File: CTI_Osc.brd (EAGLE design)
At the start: 53 x 45 mm, 15 parts, among them IC6 7805DT

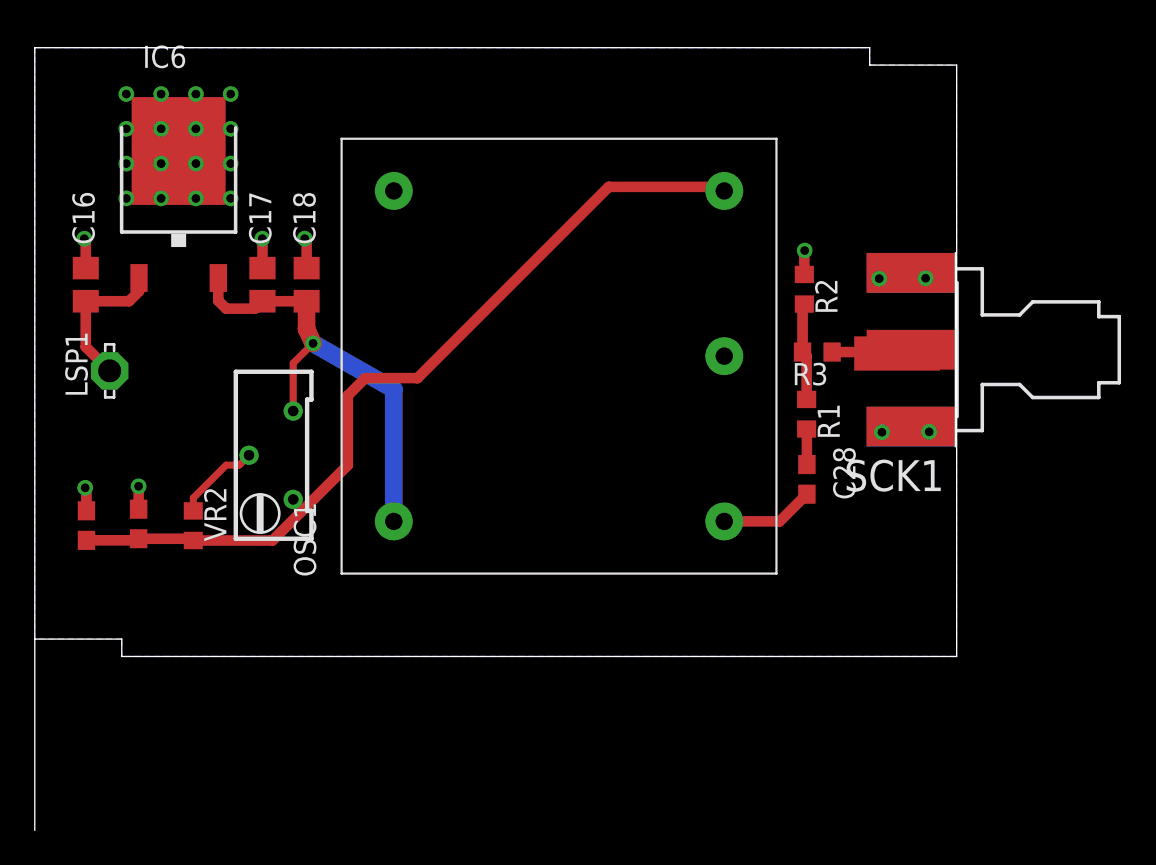
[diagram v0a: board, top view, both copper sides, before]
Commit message: V1 release
Added a TL431C for precision control of the freq set pin.
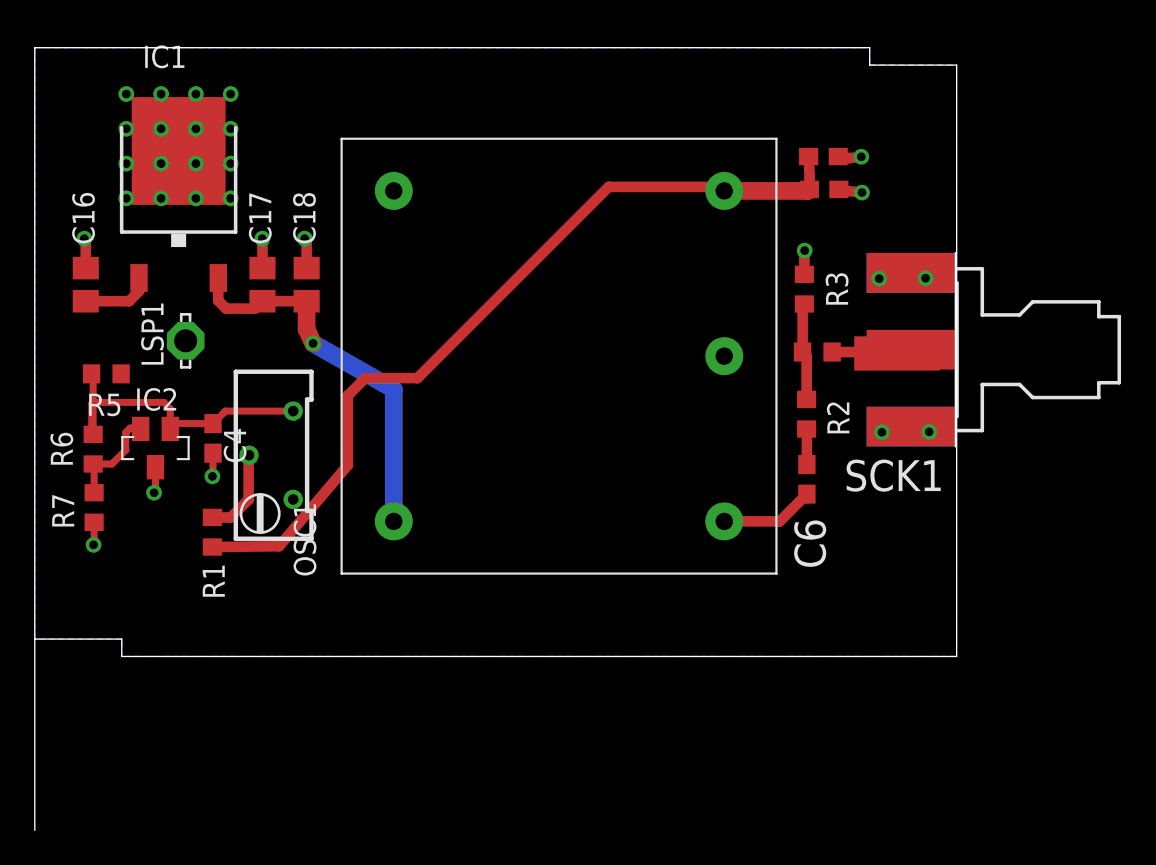
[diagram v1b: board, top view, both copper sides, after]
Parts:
- added C4: 100nF, rcl:C0603
- added IC2: TL431AIDBZR, RF:SOT23L
- added R5, R6, R7: 10K, rcl:R0603
- moved C24 46.6 mm to (45.4, 26.8), turned to 0 degrees
- moved C25 44.7 mm to (45.3, 28.7), turned to 0 degrees
- moved LSP1 4.70 mm to (8.67, 18.1)
- moved R13 1.16 mm to (10.2, 7.14)
- renumbered IC6 to IC1
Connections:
- new net +5V_PRECISION: C4.1, IC2.G, R5.2, R6.2, VR2.3
- new net N$42: IC2.S, R6.1, R7.2
- net +12V: now also R5.1
- net +5V: no longer VR2.3
- net GND: now also C4.2, IC2.D, R7.1
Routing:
- net +5V_PRECISION: track 0.00 -> 18.7 mm
- net N$42: track 0.00 -> 5.88 mm
- net +12V: track 8.65 -> 4.07 mm
- net +5V: track 26.6 -> 22.2 mm
- net GND: track 9.21 -> 13.4 mm, vias 26 -> 29
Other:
- board text added: "C6"
